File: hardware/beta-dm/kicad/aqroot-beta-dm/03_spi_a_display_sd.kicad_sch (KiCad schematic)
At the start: 18 parts, among them J1 CH280QV10-CT_50P, J2 Molex_5025700893, U17 TPS61169DCKR

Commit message: Beta-DM: finalize JLC component matching and manual-source plan
Both CTO rulings applied, the two remaining engineering gates closed with real
manufacturer data, and the E list is empty.

D8. The old lock NSR0240V2T5G is a SOD-523 part and the land is SOD-323, so it
never fitted - a defect in our own ledger that only surfaced because JLC's
matcher suggested the package-correct sibling. Now locked to onsemi
NSR0240HT1G, SOD-323, 40 V, 250 mA Schottky. It is NOT pinned to a JLC code:
C152519 shows 13 in stock against a 116-piece minimum purchase and a negative
presale balance, so it cannot be bought today. Pinning an unbuyable code only
fails at checkout. Manual source; two pieces of a 2-pin SOD-323 are trivial.

SW1-SW8. All eight locked to one part, C&K PTS645SM43SMTR92LFS / C221880,
1.6 N, SMD-4P 6x6 mm gull wing, 4.3 mm actuator, stock 8462. The 'x' in
PTS645Sx43SMTR92 was always the actuation-force letter and the design had never
fixed it; M = 1.6 N is the Beta-DM feel baseline, revisitable after hands-on
testing. JLC's lone hanxia match for SW5 is rejected - it would have made one
button differ from the other seven.

C26/C27 hard gate: PASS. Murata GRM31CR71E106KA12L, 10 uF 25 V X7R 1206,
C77093, stock 226763. TI SLUSF65A 8.2.2.3 also asks for 25 V parts on IN/SYS.
Official Murata SimSurfing data at 25 degC / AC 1 Vrms: 10.923 uF at 0 V and
9.000 uF at 4.5 V, a change of -17.60 %. Per capacitor that is 9.00 uF against
the >=5 uF floor and 18.0 uF combined against the >=10 uF floor, 1.80x both.
With -10 % tolerance, 8.10 uF each and 16.2 uF combined, 1.62x both; with X7R
-15 % temperature on top, 6.885 uF and 13.77 uF, 1.38x both. The obsolete
GRM21BR71A106KE51L was never a candidate.

R32/R35/R42 closed with numbers rather than judgement. The netlist shows R35 is
the only power-node jumper of the three - it bridges USB_VBUS_RAW to
USB_VBUS_CHG, while R32 is a shield tie and R42 a PS/SYNC strap. The rule text
names R42 as the power node; the netlist says R35, and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
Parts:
- D8: MPN NSR0240V2T5G -> NSR0240HT1G
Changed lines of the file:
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@@
 			)
 		)
-		(property "MPN" "NSR0240V2T5G"
+		(property "MPN" "NSR0240HT1G"
 			(at 247.65 135.89 0)
 			(hide yes)

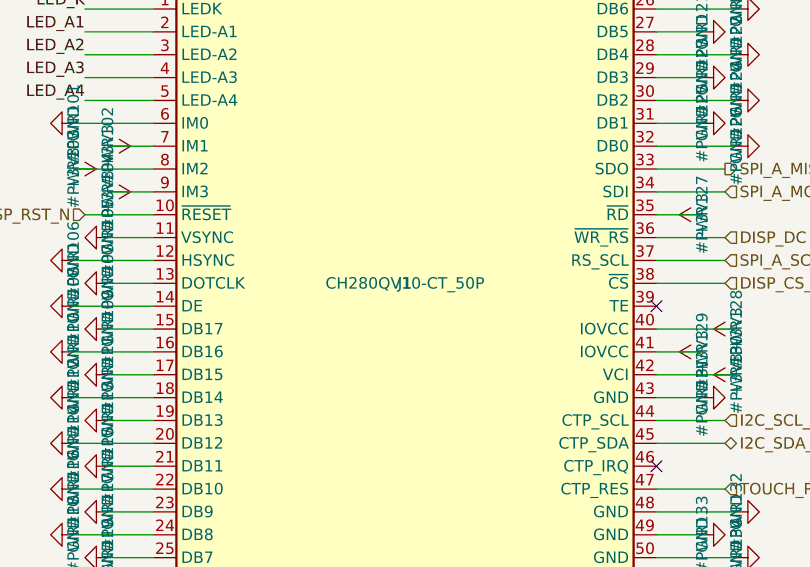
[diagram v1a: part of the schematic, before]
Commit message: Beta-DM: J1 is the Hirose FPC connector, not the display module
J1's procurement metadata named CH280QV10-CT - a ChengHao 2.8 inch TFT plus
capacitive-touch DISPLAY MODULE - while its footprint has always been
AQROOT_Beta:Hirose_FH69-50S-0.5SH. Two different physical items had been
collapsed into one BOM line, and every earlier pass duly searched JLC for the
display, found it discontinued, and filed J1 as manual source.

J1 is the PCB-side FPC connector: Hirose FH69-50S-0.5SH, HRS No.
CL0580-5008-0-00. JLC stocks it - C25955556, HRS(Hirose), 1072 pieces, minimum
purchase 1, USD 1.6944 - and JLC's description matches the footprint's own
documentation line for line: 50P, 0.5 mm pitch, surface mount right angle,
double-sided top and bottom entry, front insertion and back flip, 500 mA, 50 V,
-55 to +125 C. Digi-Key and Mouser both list it, around USD 1.62, so it is an
active mainstream part rather than a JLC-only listing.

Compatibility was re-checked rather than assumed. The land was already
VERIFIED_VENDOR_EXACT from the 2026-08-08 pass and was re-measured this pass
straight out of the board against the Hirose catalogue Recommended PCB Layout:
50 signal pads 0.30 x 1.23 on 0.5 pitch spanning C = 24.5, hold-downs 0.36 x
4.25 at x = +/-14.365 so E = 28.73 centre-to-centre, 1.90 gap, overall depth
7.38. The vertical stack closes exactly. Every value matches.

Panel side passes on every checkable item: 50 contacts against 50 positions,
0.5 mm pitch both, and a contact span of 24.5 mm arrived at independently from
the panel drawing and the connector catalogue. Contact orientation is explicitly
not a blocker because FH69 is top-and-bottom 2-point. Current has 6x margin on
the worst contact. One item stays VERIFY and is unchanged from the earlier pass:
SPEC-CH280QV10-CT_Rev.D does not state its FPC tail thickness anywhere in 18
pages, so confirm 0.30 +/-0.05 mm with a >=0.3 mm glass-epoxy stiffener against
a sample before displays are ordered. That is a panel-side measuremen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
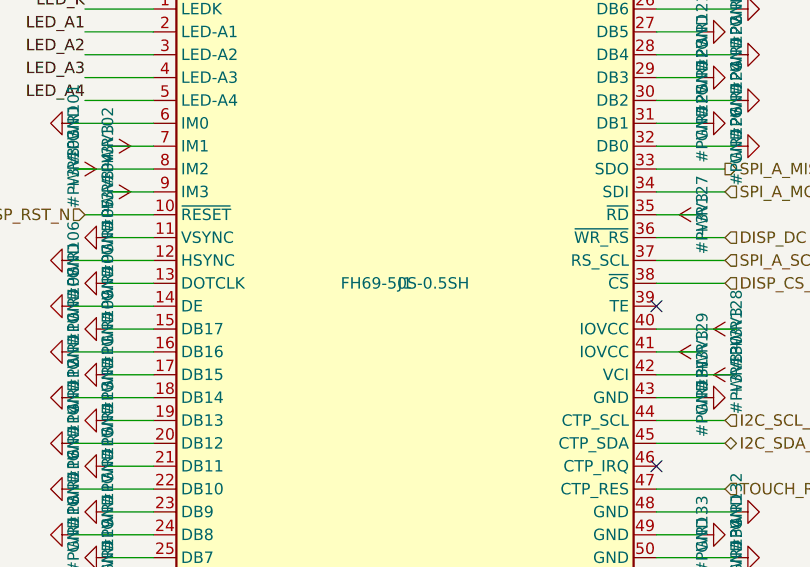
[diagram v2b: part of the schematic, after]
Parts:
- J1: value CH280QV10-CT_50P -> FH69-50S-0.5SH; MPN CH280QV10-CT -> FH69-50S-0.5SH; Manufacturer Shenzhen ChengHao Optoelectronic -> Hirose
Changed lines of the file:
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@@
 			)
 		)
-		(property "Value" "CH280QV10-CT_50P"
+		(property "Value" "FH69-50S-0.5SH"
 			(at 95.25 148.59 0)
 			(effects
@@
 			)
 		)
-		(property "Manufacturer" "Shenzhen ChengHao Optoelectronic"
+		(property "Manufacturer" "Hirose"
 			(at 95.25 148.59 0)
 			(hide yes)
@@
 			)
 		)
-		(property "MPN" "CH280QV10-CT"
+		(property "MPN" "FH69-50S-0.5SH"
 			(at 95.25 148.59 0)
 			(hide yes)
